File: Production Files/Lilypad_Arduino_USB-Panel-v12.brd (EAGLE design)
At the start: 125.7 x 125.7 mm, 183 parts, among them U1 MCP73831, U10 ATMEGA32U41:1, U11 MCP73831, U12 MIC5219, U2 MIC5219, U3 ATMEGA32U41:1, U4 ATMEGA32U41:1, U5 MCP73831, U6 MIC5219, U7 ATMEGA32U41:1, U8 MCP73831, U9 MIC5219, Y1 8MHz, Y2 8MHz, Y3 8MHz, Y4 8MHz

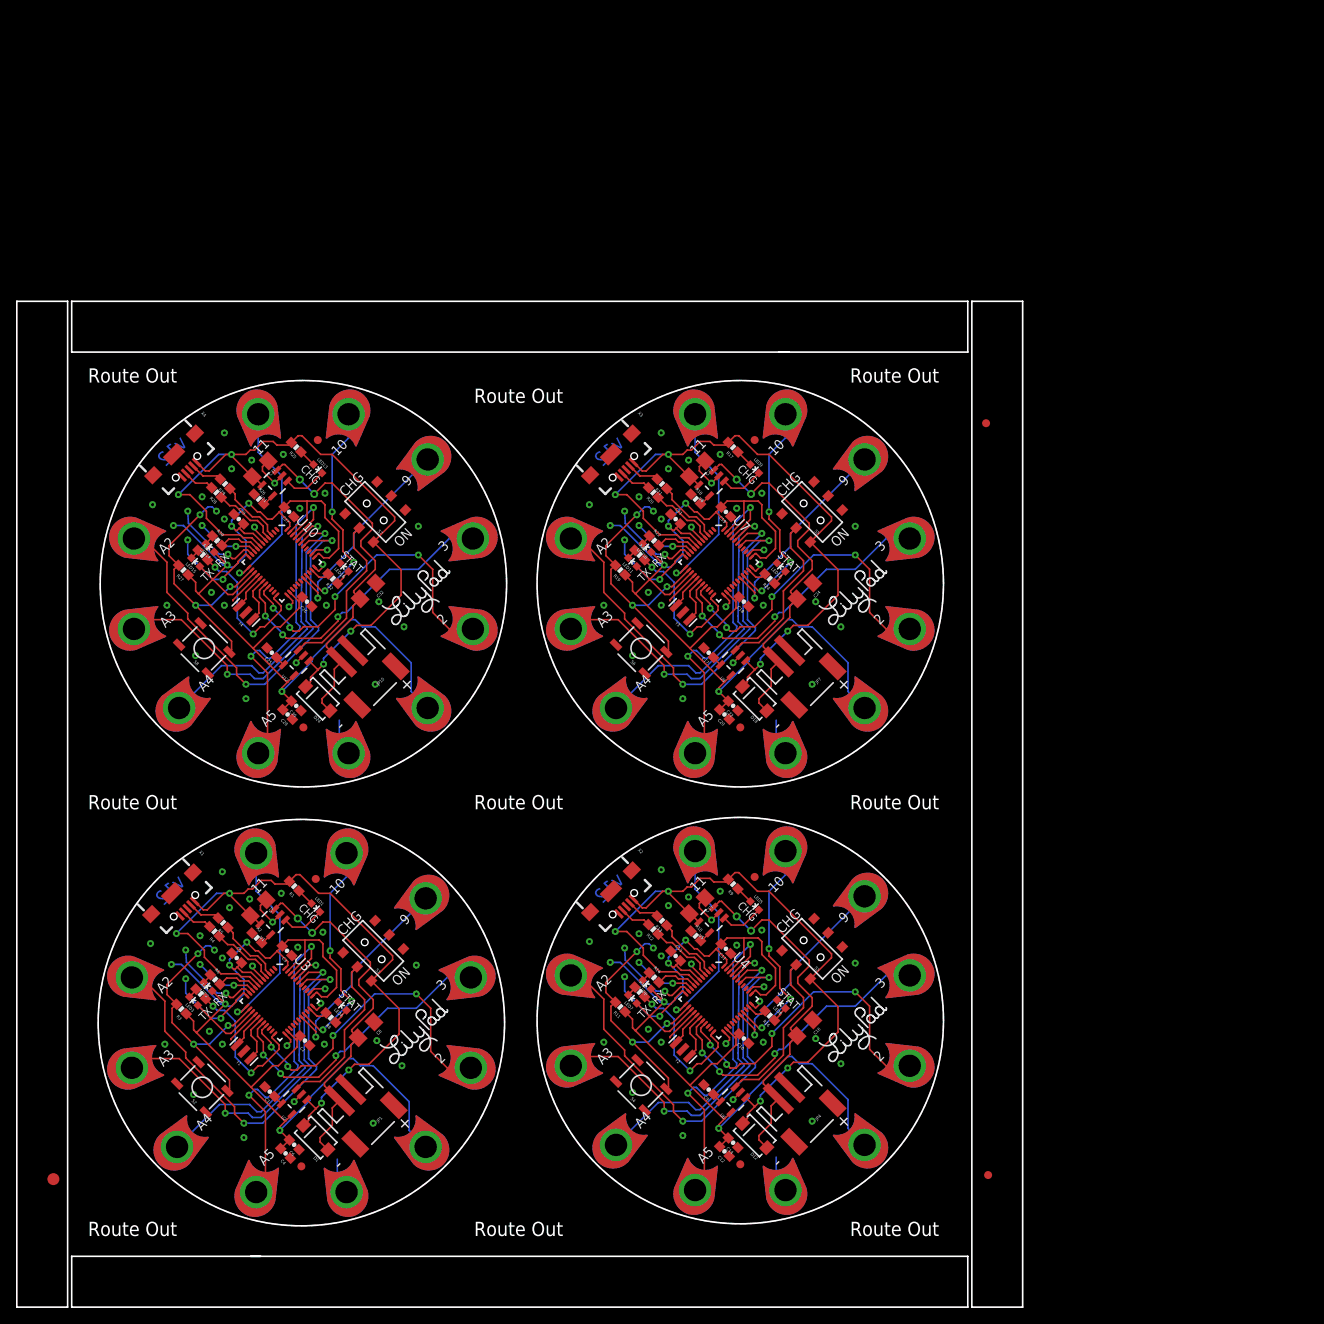
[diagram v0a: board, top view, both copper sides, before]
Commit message: Re-created Panel
Re-created panel v12
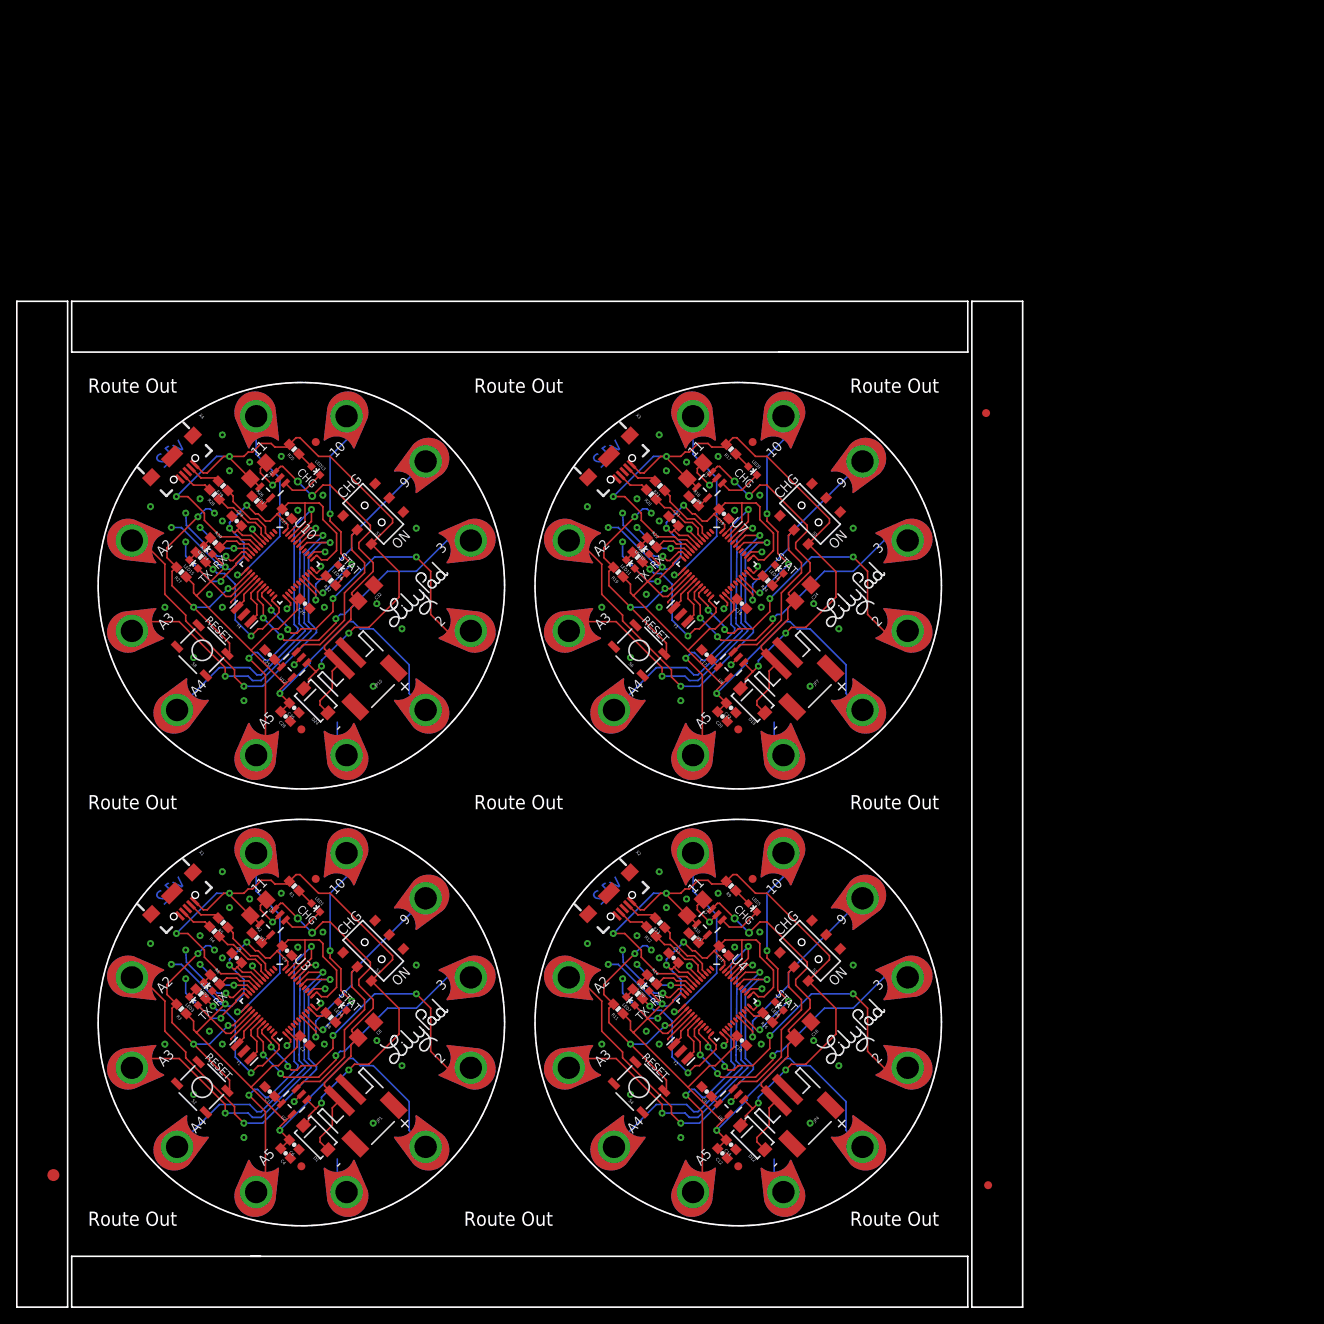
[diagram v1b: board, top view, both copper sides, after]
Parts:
- added U$12: LOGO-LPLP, LilyPad-Wearables:LOGO-LILYPAD
- added U$14: LOGO-LPLPA, LilyPad-Wearables:LOGO-LPA
- added U$15: OSHW-LOGOM, SparkFun:OSHW-LOGO-M
- added U$16: (no value), SparkFun-Aesthetics:SFE-LOGO-FLAME
- U$10: value LOGO-LPLPA -> OSHW-LOGOM; device LilyPad-Wearables:LOGO-LPA -> SparkFun:OSHW-LOGO-M
- U$11: value OSHW-LOGOM -> (none); device SparkFun:OSHW-LOGO-M -> SparkFun-Aesthetics:SFE-LOGO-FLAME
- U$6: value LOGO-LPLP -> (none); device LilyPad-Wearables:LOGO-LILYPAD -> SparkFun-Aesthetics:SFE-LOGO-FLAME
- U$7: value LOGO-LPLPA -> (none); device LilyPad-Wearables:LOGO-LPA -> SparkFun-Aesthetics:SFE-LOGO-FLAME
- U$8: value OSHW-LOGOM -> LOGO-LPLP; device SparkFun:OSHW-LOGO-M -> LilyPad-Wearables:LOGO-LILYPAD
- U$9: value LOGO-LPLP -> LOGO-LPLPA; device LilyPad-Wearables:LOGO-LILYPAD -> LilyPad-Wearables:LOGO-LPA
- moved U$6 87.2 mm to (-1.43, 2.52), flipped to the bottom, turned to 315 degrees
- moved U$11 59.3 mm to (53.2, 57.1)
- moved U$7 52.4 mm to (53.2, 2.52)
- moved U$10 48.4 mm to (48.3, 60.9)
- moved U$9 40.1 mm to (54.6, 54.6), flipped to the bottom, turned to 315 degrees
- moved U$8 21.7 mm to (68.9, 53.5), flipped to the top, turned to 45 degrees
- moved E$4 1.27 mm to (85.9, -20.3)
- moved E$5 1.27 mm to (85.6, 76.2)
- moved E$1 0.51 mm to (-31.0, -19.1)
- moved A11 0.35 mm to (49.0, 33.4)
- moved A7 0.35 mm to (49.0, -21.2)
- moved -3 0.35 mm to (5.67, 33.4)
- moved A15 0.35 mm to (-5.65, 33.4)
- moved -2 0.35 mm to (60.3, 33.4)
- moved -1 0.35 mm to (60.3, -21.2)
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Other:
- outline, holes or cut-outs redrawn
- board text added: "RESET"

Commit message: created panel v12
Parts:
- removed E$4: (no value), SparkFun-Aesthetics:FIDUCIAL-1X2
- removed X1, X2, X3, X4: (no value), Testing:USB-AB-MICRO-SMD_V03
- added E$3: (no value), SparkFun-Aesthetics:FIDUCIAL-1X2
- added U13: ATMEGA32U41:1-LESS_PASTE, Testing:QFN-44-NOPAD_1:1-LESS_PASTE
- added U14: MCP73831, SparkFun-PowerIC:SOT23-5
- added U15: MIC5219, SparkFun-PowerIC:SOT23-5
- added U16: (no value), SparkFun-Connectors:USB-AB-MICRO-SMD_V03
- E$1: device SparkFun-Aesthetics:FIDUCIAL-1.5X3 -> SparkFun-Retired:FIDUCIAL-1.5X3
- S1, S3, S5, S7: value SWITCH-DPDTSMD -> (none)
- U$11, U$16, U$6, U$7: device SparkFun-Aesthetics:SFE-LOGO-FLAME -> SparkFun-Aesthetics:SFE_LOGO_FLAME_.2
- U10: value ATMEGA32U41:1 -> MCP73831; device Testing:QFN-44-NOPAD_1:1 -> SparkFun-PowerIC:SOT23-5
- U11: value MCP73831 -> MIC5219
- U12: value MIC5219 -> (none); device SparkFun-PowerIC:SOT23-5 -> SparkFun-Connectors:USB-AB-MICRO-SMD_V03
- U3, U4: value ATMEGA32U41:1 -> ATMEGA32U41:1-LESS_PASTE; device Testing:QFN-44-NOPAD_1:1 -> Testing:QFN-44-NOPAD_1:1-LESS_PASTE
- U5, U8: value MCP73831 -> (none); device SparkFun-PowerIC:SOT23-5 -> SparkFun-Connectors:USB-AB-MICRO-SMD_V03
- U6: value MIC5219 -> MCP73831
- U7: value ATMEGA32U41:1 -> MIC5219; device Testing:QFN-44-NOPAD_1:1 -> SparkFun-PowerIC:SOT23-5
- U9: value MIC5219 -> ATMEGA32U41:1-LESS_PASTE; device SparkFun-PowerIC:SOT23-5 -> Testing:QFN-44-NOPAD_1:1-LESS_PASTE
- moved U$6 101.4 mm to (92.5, 40.6)
- moved U10 100.3 mm to (86.8, 102.7), turned to 135 degrees
- moved U12 97.1 mm to (74.2, 106.3), turned to 315 degrees
- moved U11 94.0 mm to (89.5, 80.3)
- moved U6 66.8 mm to (86.8, 48.1)
- moved U9 58.9 mm to (87.7, 92.9), turned to 315 degrees
- moved U$16 54.7 mm to (37.9, 95.2)
- moved U$11 54.7 mm to (92.5, 95.2)
- moved S2 51.3 mm to (24.0, 28.1)
- moved S4 51.3 mm to (78.6, 28.1)
- moved S6 51.3 mm to (78.6, 82.7)
- moved S8 51.3 mm to (24.0, 82.7)
- moved E$1 51.2 mm to (4.57, 17.8)
- moved JP11 50.4 mm to (35.8, 72.2)
- moved R19 50.4 mm to (75.4, 91.9)
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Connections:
- removed net N$23 (its old number): S3.2, U6.3
- removed net N$27 (its old number): C9.1, U6.4
- removed net N$36 (its old number): R12.2, X2.ID1
- removed net N$44 (its old number): X2.D+1
- removed net N$57 (its old number): R21.2, X3.D-1
- removed net N$58 (its old number): R20.2, X3.ID1
- removed net N$63 (its old number): D13.1, U7.19
- removed net N$78 (its old number): A13.1, U10.38
- removed net N$79 (its old number): R29.2, X4.D-1
- removed net N$84 (its old number): U10.16, Y4.3
- removed net N$85: D19.1, U10.19
- removed net N$86: D21.1, U10.18
- removed net N$88: X4.D+1
- new net N$24: LED5.C, U6.1
- new net N$34: R13.2, U8.D-1
- new net N$43: S5.2, U11.3
- new net N$46: R18.2, U10.5
- new net N$59: U9.17, Y3.1
- new net N$60: U9.16, Y3.3
- new net N$68: C25.1, U15.4
- new net N$81: U13.16, Y4.3
- new net N$82: D19.1, U13.19
- net 3.3V1: now also U7.5; no longer U6.5
- net 3.3V2: now also U11.5, U9.14, U9.24, U9.34, U9.42, U9.44, U9.6; no longer U7.14, U7.24, U7.34, U7.42, U7.44, U7.6, U9.5
- net 3.3V3: now also U13.14, U13.24, U13.34, U13.42, U13.44, U13.6, U15.5; no longer U10.14, U10.24, U10.34, U10.42, U10.44, U10.6, U12.5
- net 5V: now also U5.VBUS1; no longer X1.VBUS1
- net 5V1: now also U6.4, U7.1, U8.VBUS1; no longer U5.4, U6.1, X2.VBUS1
- net 5V2: now also U10.4, U11.1, U12.VBUS1, U9.7; no longer U7.7, U8.4, U9.1, X3.VBUS1
- net 5V3: now also U13.7, U14.4, U15.1, U16.VBUS1; no longer U10.7, U11.4, U12.1, X4.VBUS1
- net D+2: now also U9.4; no longer U7.4
- net D+3: now also U13.4; no longer U10.4
- net D-2: now also U9.3; no longer U7.3
- net D-3: now also U13.3; no longer U10.3
- net GND: now also U5.GND1; no longer X1.GND1
- net GND1: now also U7.2, U8.GND1; no longer U5.2, X2.GND1
- net GND2: now also U10.2, U11.2, U12.GND1, U9.15, U9.23, U9.33, U9.35, U9.43, U9.5; no longer U7.15, U7.23, U7.33, U7.35, U7.43, U7.5, U8.2, U9.2, X3.GND1
- net GND3: now also U13.15, U13.23, U13.33, U13.35, U13.43, U13.5, U14.2, U15.2, U16.GND1; no longer U10.15, U10.23, U10.33, U10.35, U10.43, U10.5, U11.2, U12.2, X4.GND1
- net MISO2: now also U9.11; no longer U7.11
- net MISO3: now also U13.11; no longer U10.11
- net MOSI2: now also U9.10; no longer U7.10
- net MOSI3: now also U13.10; no longer U10.10
- net N$19: now also U5.D-1; no longer X1.D-1
- net N$20: now also U5.D+1; no longer X1.ID1
- net N$22: now also S3.2, U7.3; no longer X1.D+1
- net N$25: now also R10.2, U6.5; no longer LED5.C, U5.1
- net N$26: now also C9.1, U7.4; no longer R10.2, U5.5
- net N$35: now also R12.2, U8.D+1; no longer R13.2, X2.D-1
- net N$45: now also LED9.C, U10.1; no longer S5.2, U9.3
- net N$47: now also C17.1, U11.4; no longer LED9.C, U8.1
- net N$48: now also D17.1, U9.12; no longer R18.2, U8.5
- net N$49: now also D16.1, U9.30; no longer C17.1, U9.4
- net N$50: now also D14.1, U9.29; no longer D17.1, U7.12
- net N$51: now also A11.1, U9.41; no longer D16.1, U7.30
- net N$52: now also A12.1, U9.40; no longer D14.1, U7.29
- net N$53: now also A10.1, U9.39; no longer A11.1, U7.41
- net N$54: now also A9.1, U9.38; no longer A12.1, U7.40
- net N$55: now also R21.2, U12.D-1; no longer A10.1, U7.39
- net N$56: now also R20.2, U12.D+1; no longer A9.1, U7.38
- net N$61: now also D13.1, U9.19; no longer U7.17, Y3.1
- net N$62: now also D15.1, U9.18; no longer U7.16, Y3.3
- net N$64: now also S7.2, U15.3; no longer D15.1, U7.18
- net N$66: now also LED13.C, U14.1; no longer X3.D+1
- net N$67: now also R26.2, U14.5; no longer S7.2, U12.3
- net N$69: now also D23.1, U13.12; no longer LED13.C, U11.1
- net N$70: now also D22.1, U13.30; no longer R26.2, U11.5
- net N$71: now also D20.1, U13.29; no longer C25.1, U12.4
- net N$72: now also A15.1, U13.41; no longer D23.1, U10.12
- net N$73: now also A16.1, U13.40; no longer D22.1, U10.30
- net N$74: now also A14.1, U13.39; no longer D20.1, U10.29
- net N$75: now also A13.1, U13.38; no longer A15.1, U10.41
- net N$76: now also R29.2, U16.D-1; no longer A16.1, U10.40
- net N$77: now also R28.2, U16.D+1; no longer A14.1, U10.39
- net N$80: now also U13.17, Y4.1; no longer R28.2, X4.ID1
- net N$83: now also D21.1, U13.18; no longer U10.17, Y4.1
- net RESET2: now also U9.13; no longer U7.13
- net RESET3: now also U13.13; no longer U10.13
- net RX_LED2: now also U9.8; no longer U7.8
- net RX_LED3: now also U13.8; no longer U10.8
- net SCK2: now also U9.9; no longer U7.9
- net SCK3: now also U13.9; no longer U10.9
- net TX_LED2: now also U9.22; no longer U7.22
- net TX_LED3: now also U13.22; no longer U10.22
- net USER_LED2: now also U9.32; no longer U7.32
- net USER_LED3: now also U13.32; no longer U10.32
- net V_BATT1: now also U6.3; no longer U5.3
- net V_BATT2: now also U10.3; no longer U8.3
- net V_BATT3: now also U14.3; no longer U11.3
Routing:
- net N$78 (its old number): track 53.9 -> 0.00 mm, vias 2 -> 0
- net N$56: track 53.9 -> 3.72 mm, vias 2 -> 0
- net N$77: track 45.9 -> 3.72 mm, vias 2 -> 0
- net N$55: track 45.9 -> 4.08 mm, vias 2 -> 0
- net N$85: track 41.6 -> 0.00 mm, vias 4 -> 0
- net N$63 (its old number): track 41.6 -> 0.00 mm, vias 4 -> 0
- net N$82: track 0.00 -> 41.6 mm, vias 0 -> 4
- net N$86: track 37.3 -> 0.00 mm, vias 3 -> 0
- net N$61: track 5.90 -> 41.6 mm, vias 0 -> 4
- net N$76: track 38.4 -> 4.08 mm, vias 1 -> 0
- net N$62: track 4.52 -> 37.3 mm, vias 0 -> 3
- net N$83: track 5.90 -> 37.3 mm, vias 0 -> 3
- net N$70: track 1.54 -> 28.7 mm, vias 0 -> 3
- net N$49: track 2.71 -> 28.7 mm, vias 0 -> 3
- net N$71: track 2.71 -> 26.2 mm, vias 0 -> 1
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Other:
- outline, holes or cut-outs redrawn
- board text removed: "Route Out"
